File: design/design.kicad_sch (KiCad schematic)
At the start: 9 parts, among them J1 Conn_01x03_Pin, U1 MC7912, U2 L7812

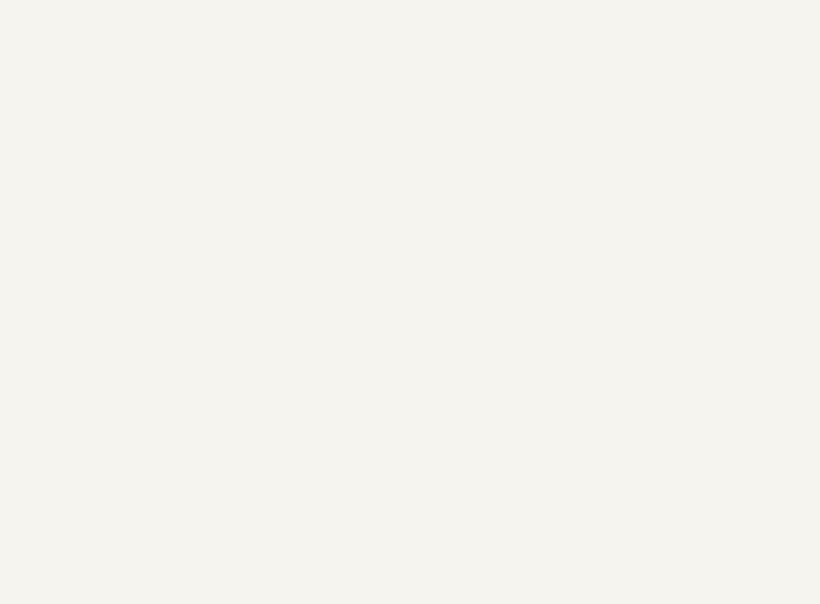
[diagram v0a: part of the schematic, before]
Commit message: Algunos datasheet nuevos
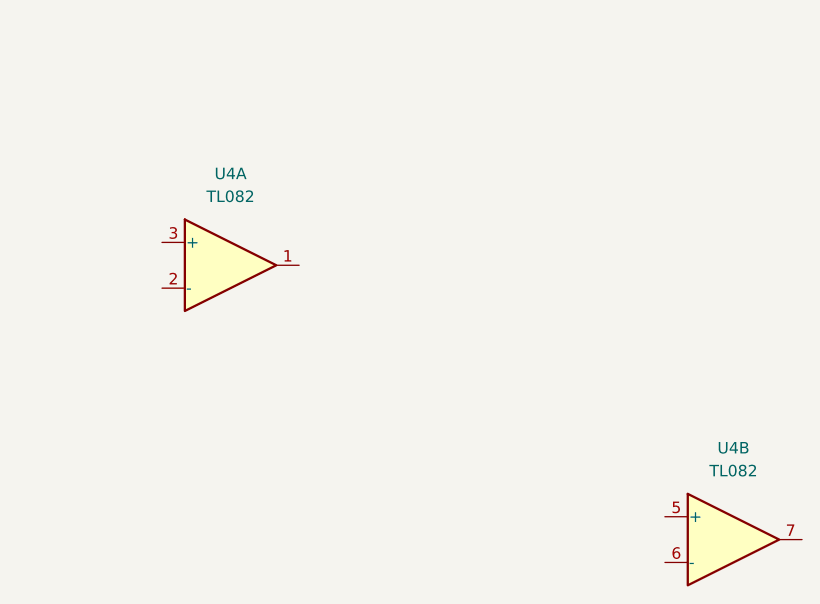
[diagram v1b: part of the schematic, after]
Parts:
- added U4: TL082, symbol Amplifier_Operational:TL082
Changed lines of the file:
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@@
+    )
+  )
+  (symbol (lib_id "Amplifier_Operational:TL082") (at 135.89 67.31 0) (unit 1)
+    (in_bom yes) (on_board yes) (dnp no) (fields_autoplaced)
+    (property "Reference" "U4" (at 135.89 57.15 0)
+      (effects (font (size 1.27 1.27)))
+    )
+    (property "Value" "TL082" (at 135.89 59.69 0)
+      (effects (font (size 1.27 1.27)))
+    )
+    (property "Footprint" "" (at 135.89 67.31 0)
+      (effects (font (size 1.27 1.27)) hide)
+    )
+    (property "Datasheet" "http://www.ti.com/lit/ds/symlink/tl081.pdf" (at 135.89 67.31 0)
+      (effects (font (size 1.27 1.27)) hide)
+    )
+    (pin "1")
+    (pin "2")
+    (pin "3")
+    (pin "5")
+    (pin "6")
+    (pin "7")
+    (pin "4")
+    (pin "8")
+    (instances
+      (project "design"
+        (path "/a520f27b-3eb4-44e7-9faf-250bc52b55ee"
+          (reference "U4") (unit 1)
+        )
+      )
     )
   )
@@
         )
       )
+    )
+  )
+  (symbol (lib_id "Amplifier_Operational:TL082") (at 191.77 97.79 0) (unit 2)
+    (in_bom yes) (on_board yes) (dnp no) (fields_autoplaced)
+    (property "Reference" "U4" (at 191.77 87.63 0)
+      (effects (font (size 1.27 1.27)))
+    )
+    (property "Value" "TL082" (at 191.77 90.17 0)
+      (effects (font (size 1.27 1.27)))
+    )
+    (property "Footprint" "" (at 191.77 97.79 0)
+      (effects (font (size 1.27 1.27)) hide)
+    )
+    (property "Datasheet" "http://www.ti.com/lit/ds/symlink/tl081.pdf" (at 191.77 97.79 0)
+      (effects (font (size 1.27 1.27)) hide)
+    )
+    (pin "1")
+    (pin "2")
+    (pin "3")
+    (pin "5")
+    (pin "6")
+    (pin "7")
+    (pin "4")
+    (pin "8")
+    (instances
+      (project "design"
+        (path "/a520f27b-3eb4-44e7-9faf-250bc52b55ee"
+          (reference "U4") (unit 2)
+        )
+      )
